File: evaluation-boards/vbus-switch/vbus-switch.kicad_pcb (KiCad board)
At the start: 4 copper layers, 74 x 59 mm, 83 parts, among them J1 BANANA, J10 01x02, J11 Conn_02x06_Top_Bottom, J2 BANANA, J3 BANANA, J4 USB_C, J5 USB_C, J6 USB_A, J7 01x02, J8 01x02, J9 01x02, Q1 PMOS, Q2 PMOS, Q3 PMOS, Q4 PMOS, Q5 2PMOS, Q6 2NMOS, Q7 2NMOS, U1 PAC195X-1-WLCSP, U2 FUSB302BMPX

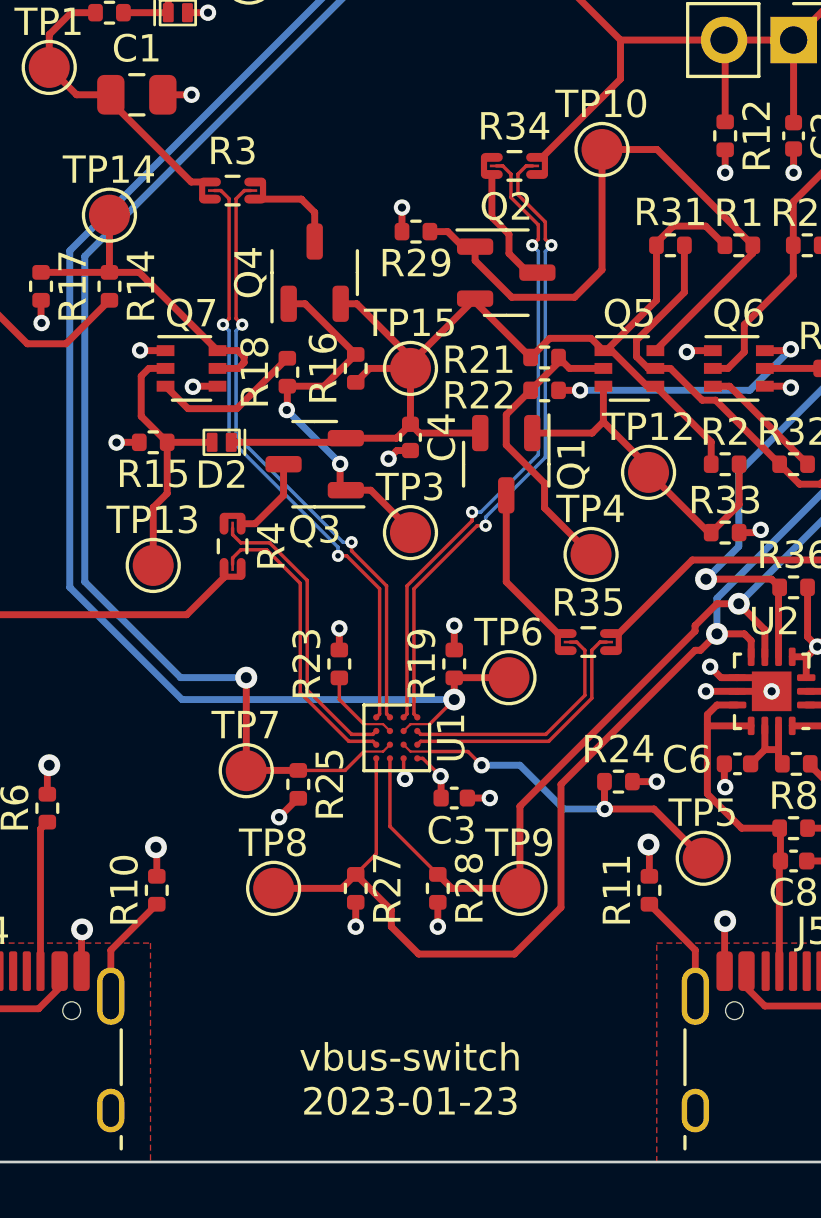
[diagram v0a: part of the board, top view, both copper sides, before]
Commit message: vbus-switch: up minimum trace/space to 3.5 mil
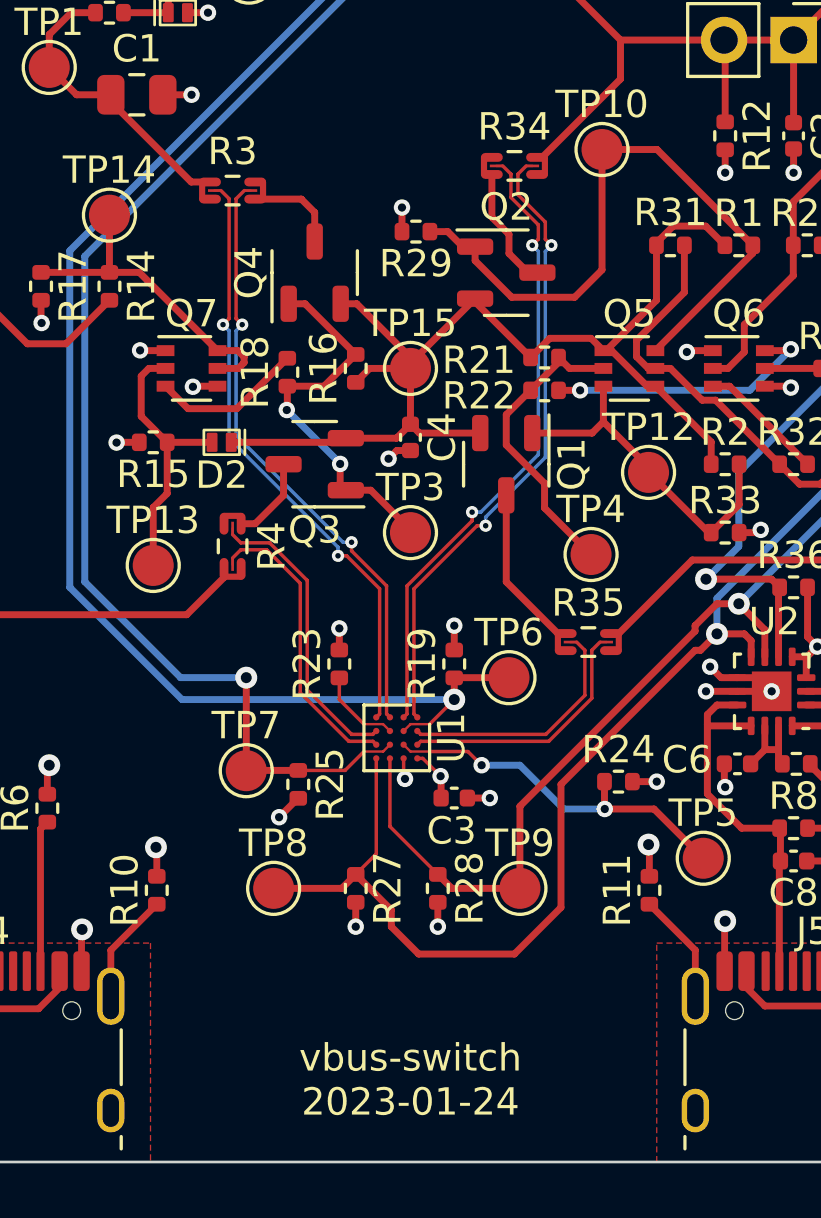
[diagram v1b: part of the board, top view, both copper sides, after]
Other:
- board text added: "vbus-switch 2023-01-24"
- board text removed: "vbus-switch 2023-01-23"
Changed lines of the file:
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@@
     (effects (font (size 2 2) (thickness 0.3)))
   )
-  (gr_text "vbus-switch\n2023-01-23" (at 150 119) (layer "F.SilkS")
+  (gr_text "vbus-switch\n2023-01-24" (at 150 119) (layer "F.SilkS")
     (effects (font (size 1 1) (thickness 0.15)))
   )
@@
   (segment (start 143.92 92.58) (end 143.69 92.35) (width 0.254) (layer "F.Cu") (net 35))
   (segment (start 147.4 104.31) (end 147.4 105.1) (width 0.127) (layer "F.Cu") (net 36))
-  (segment (start 149 106) (end 148.3 106) (width 0.083) (layer "F.Cu") (net 36))
-  (segment (start 149.25 106.25) (end 149 106) (width 0.083) (layer "F.Cu") (net 36))
+  (segment (start 149 106) (end 148.3 106) (width 0.0889) (layer "F.Cu") (net 36))
   (segment (start 147.4 105.1) (end 148.3 106) (width 0.127) (layer "F.Cu") (net 36))
+  (segment (start 149.25 106.25) (end 149 106) (width 0.0889) (layer "F.Cu") (net 36))
   (segment (start 157.1 109.1) (end 158.9 109.1) (width 0.254) (layer "F.Cu") (net 37))
-  (segment (start 149.75 106.75) (end 150 107) (width 0.083) (layer "F.Cu") (net 37))
+  (segment (start 149.75 106.75) (end 150 107) (width 0.0889) (layer "F.Cu") (net 37))
   (segment (start 152.6 107.5) (end 152.1 107) (width 0.127) (layer "F.Cu") (net 37))
-  (segment (start 150 107) (end 150.7 107) (width 0.083) (layer "F.Cu") (net 37))
+  (segment (start 150 107) (end 150.7 107) (width 0.0889) (layer "F.Cu") (net 37))
   (segment (start 157.09 109.09) (end 157.1 109.1) (width 0.254) (layer "F.Cu") (net 37))
   (segment (start 158.9 109.1) (end 160.7 110.9) (width 0.254) (layer "F.Cu") (net 37))
@@
   (segment (start 160.8 100.7) (end 162 99.5) (width 0.254) (layer "B.Cu") (net 41))
   (segment (start 151.6 105.1) (end 150.7 106) (width 0.127) (layer "F.Cu") (net 42))
-  (segment (start 149.75 106.25) (end 150 106) (width 0.083) (layer "F.Cu") (net 42))
+  (segment (start 149.75 106.25) (end 150 106) (width 0.0889) (layer "F.Cu") (net 42))
   (segment (start 153.6 104.3) (end 151.61 104.3) (width 0.254) (layer "F.Cu") (net 42))
   (segment (start 151.6 104.31) (end 151.6 105.1) (width 0.254) (layer "F.Cu") (net 42))
-  (segment (start 150 106) (end 150.7 106) (width 0.083) (layer "F.Cu") (net 42))
+  (segment (start 150 106) (end 150.7 106) (width 0.0889) (layer "F.Cu") (net 42))
   (segment (start 151.61 104.3) (end 151.6 104.31) (width 0.254) (layer "F.Cu") (net 42))
   (via (at 151.6 105.1) (size 0.8) (drill 0.4) (layers "F.Cu" "B.Cu") (net 42))
@@
   (segment (start 145.9 107.69) (end 147.61 107.69) (width 0.127) (layer "F.Cu") (net 43))
   (segment (start 144 107.7) (end 144.01 107.69) (width 0.254) (layer "F.Cu") (net 43))
-  (segment (start 149.25 106.75) (end 149 107) (width 0.083) (layer "F.Cu") (net 43))
+  (segment (start 149.25 106.75) (end 149 107) (width 0.0889) (layer "F.Cu") (net 43))
   (segment (start 144 104.3) (end 144 107.7) (width 0.254) (layer "F.Cu") (net 43))
-  (segment (start 149 107) (end 148.3 107) (width 0.083) (layer "F.Cu") (net 43))
+  (segment (start 149 107) (end 148.3 107) (width 0.0889) (layer "F.Cu") (net 43))
   (segment (start 147.61 107.69) (end 148.3 107) (width 0.127) (layer "F.Cu") (net 43))
   (via (at 144 104.3) (size 0.8) (drill 0.4) (layers "F.Cu" "B.Cu") (net 43))
@@
   (segment (start 148.872999 101.052605) (end 147.667882 99.847488) (width 0.127) (layer "F.Cu") (net 55))
   (segment (start 147.667882 99.847488) (end 147.352512 99.847488) (width 0.127) (layer "F.Cu") (net 55))
-  (segment (start 142.8375 86.5) (end 143.073 86.5) (width 0.127) (layer "F.Cu") (net 55))
+  (segment (start 142.8375 86.5) (end 143.073 86.5) (width 0.0889) (layer "F.Cu") (net 55))
   (segment (start 143.15 91.4) (end 143.372999 91.177001) (width 0.127) (layer "F.Cu") (net 55))
   (segment (start 143.372999 91.177001) (end 143.373 86.8) (width 0.127) (layer "F.Cu") (net 55))
@@
   (segment (start 149.25 105.75) (end 149.127001 105.627001) (width 0.127) (layer "F.Cu") (net 56))
   (segment (start 147.847488 99.667882) (end 147.847488 99.352512) (width 0.127) (layer "F.Cu") (net 56))
-  (segment (start 144.1625 86.5) (end 143.927 86.5) (width 0.127) (layer "F.Cu") (net 56))
+  (segment (start 144.1625 86.5) (end 143.927 86.5) (width 0.0889) (layer "F.Cu") (net 56))
   (segment (start 143.927 86.5) (end 143.627 86.8) (width 0.127) (layer "F.Cu") (net 56))
   (segment (start 149.127001 100.947395) (end 147.847488 99.667882) (width 0.127) (layer "F.Cu") (net 56))
@@
   (segment (start 146.227 100.747394) (end 144.852606 99.373) (width 0.127) (layer "F.Cu") (net 57))
   (segment (start 146.227 104.747394) (end 146.227 100.747394) (width 0.127) (layer "F.Cu") (net 57))
-  (segment (start 143.5 98.8375) (end 143.5 99.073) (width 0.127) (layer "F.Cu") (net 57))
+  (segment (start 143.5 98.8375) (end 143.5 99.073) (width 0.0889) (layer "F.Cu") (net 57))
   (segment (start 143.5 99.073) (end 143.8 99.373) (width 0.127) (layer "F.Cu") (net 57))
   (segment (start 147.852605 106.372999) (end 146.227 104.747394) (width 0.127) (layer "F.Cu") (net 57))
@@
   (segment (start 145.973 104.852606) (end 145.973 100.852606) (width 0.127) (layer "F.Cu") (net 58))
   (segment (start 147.747395 106.627001) (end 145.973 104.852606) (width 0.127) (layer "F.Cu") (net 58))
-  (segment (start 143.5 100.1625) (end 143.5 99.927) (width 0.127) (layer "F.Cu") (net 58))
+  (segment (start 143.5 100.1625) (end 143.5 99.927) (width 0.0889) (layer "F.Cu") (net 58))
   (segment (start 148.627001 106.627001) (end 147.747395 106.627001) (width 0.127) (layer "F.Cu") (net 58))
   (segment (start 152.252512 98.567882) (end 152.252512 98.252512) (width 0.127) (layer "F.Cu") (net 59))
@@
   (segment (start 153.373 85.6) (end 153.673 85.9) (width 0.127) (layer "F.Cu") (net 59))
   (segment (start 149.872999 100.947395) (end 152.252512 98.567882) (width 0.127) (layer "F.Cu") (net 59))
-  (segment (start 153.1375 85.6) (end 153.373 85.6) (width 0.127) (layer "F.Cu") (net 59))
+  (segment (start 153.1375 85.6) (end 153.373 85.6) (width 0.0889) (layer "F.Cu") (net 59))
   (segment (start 149.75 105.75) (end 149.872999 105.627001) (width 0.127) (layer "F.Cu") (net 59))
   (via (at 154.45 88.5) (size 0.45) (drill 0.2) (layers "F.Cu" "B.Cu") (net 59))
@@
   (segment (start 154.227 85.6) (end 153.927 85.9) (width 0.127) (layer "F.Cu") (net 60))
   (segment (start 154.927001 87.647395) (end 153.927 86.647394) (width 0.127) (layer "F.Cu") (net 60))
-  (segment (start 154.4625 85.6) (end 154.227 85.6) (width 0.127) (layer "F.Cu") (net 60))
+  (segment (start 154.4625 85.6) (end 154.227 85.6) (width 0.0889) (layer "F.Cu") (net 60))
   (segment (start 154.927001 88.277001) (end 154.927001 87.647395) (width 0.127) (layer "F.Cu") (net 60))
   (segment (start 155.15 88.5) (end 154.927001 88.277001) (width 0.127) (layer "F.Cu") (net 60))
@@
   (segment (start 152.747488 98.432118) (end 154.927001 96.252605) (width 0.127) (layer "B.Cu") (net 60))
   (segment (start 154.927001 88.722999) (end 155.15 88.5) (width 0.127) (layer "B.Cu") (net 60))
-  (segment (start 155.8375 103) (end 156.073 103) (width 0.127) (layer "F.Cu") (net 61))
+  (segment (start 155.8375 103) (end 156.073 103) (width 0.0889) (layer "F.Cu") (net 61))
   (segment (start 156.073 103) (end 156.373 103.3) (width 0.127) (layer "F.Cu") (net 61))
   (segment (start 150.25 106.25) (end 150.372999 106.372999) (width 0.127) (layer "F.Cu") (net 61))
@@
   (segment (start 154.947395 106.372999) (end 156.373 104.947394) (width 0.127) (layer "F.Cu") (net 61))
   (segment (start 156.373 104.947394) (end 156.373 103.3) (width 0.127) (layer "F.Cu") (net 61))
-  (segment (start 157.1625 103) (end 156.927 103) (width 0.127) (layer "F.Cu") (net 62))
+  (segment (start 157.1625 103) (end 156.927 103) (width 0.0889) (layer "F.Cu") (net 62))
   (segment (start 150.372999 106.627001) (end 155.052605 106.627001) (width 0.127) (layer "F.Cu") (net 62))
   (segment (start 150.25 106.75) (end 150.372999 106.627001) (width 0.127) (layer "F.Cu") (net 62))

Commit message: vbus-switch: add part selections
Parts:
- R20, R30: value R -> 10k
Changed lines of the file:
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@@
       (effects (font (size 1 1) (thickness 0.15)))
     )
-    (fp_text value "R" (at 0 1.17) (layer "F.Fab")
+    (fp_text value "10k" (at 0 1.17) (layer "F.Fab")
       (effects (font (size 1 1) (thickness 0.15)))
     )
@@
     (descr "SOT, 3 Pin (https://www.jedec.org/sites/default/files/docs/Mo-178D.PDF inferred 3-pin variant), generated with kicad-footprint-generator ipc_gullwing_generator.py")
     (tags "SOT TO_SOT_SMD")
+    (property "Manufacturer" "Panjit")
+    (property "Part Number" "PJA3441_R1_00001")
     (property "Sheetfile" "vbus-switch.kicad_sch")
     (property "Sheetname" "")
@@
     (descr "USB Type-C receptacle for USB 2.0 and PD, http://www.krhro.com/uploads/soft/180320/1-1P320120243.pdf")
     (tags "USB_C female connector receptacle type-c usb-2.0 usb pd")
+    (property "Manufacturer" "XKB")
+    (property "Part Number" "U262-161N-4BVC11")
     (property "Sheetfile" "vbus-switch.kicad_sch")
     (property "Sheetname" "")
@@
     (descr "SOT-363, SC-70-6")
     (tags "SOT-363 SC-70-6")
+    (property "Manufacturer" "Yangzhou Yangjie")
+    (property "Part Number" "BSS84DW")
     (property "Sheetfile" "vbus-switch.kicad_sch")
     (property "Sheetname" "")
@@
     (descr "WLCSP-16, PAC195X, pads sized for 3.5 mil trace/space")
     (tags "WLCSP BGA 16  0.5")
+    (property "Manufacturer" "Microchip")
+    (property "Part Number" "PAC1954T-E/J6CX")
     (property "Sheetfile" "vbus-switch.kicad_sch")
     (property "Sheetname" "")
@@
     (descr "WQFN, 14 Pin (https://www.onsemi.com/pub/Collateral/FUSB302B-D.PDF#page=32), generated with kicad-footprint-generator ipc_noLead_generator.py")
     (tags "WQFN NoLead")
+    (property "Manufacturer" "onsemi")
+    (property "Part Number" "FUSB302BMPX")
     (property "Sheetfile" "vbus-switch.kicad_sch")
     (property "Sheetname" "")
@@
     (descr "SOT, 3 Pin (https://www.jedec.org/sites/default/files/docs/Mo-178D.PDF inferred 3-pin variant), generated with kicad-footprint-generator ipc_gullwing_generator.py")
     (tags "SOT TO_SOT_SMD")
+    (property "Manufacturer" "Panjit")
+    (property "Part Number" "PJA3441_R1_00001")
     (property "Sheetfile" "vbus-switch.kicad_sch")
     (property "Sheetname" "")
@@
     (descr "SOT, 3 Pin (https://www.jedec.org/sites/default/files/docs/Mo-178D.PDF inferred 3-pin variant), generated with kicad-footprint-generator ipc_gullwing_generator.py")
     (tags "SOT TO_SOT_SMD")
+    (property "Manufacturer" "Panjit")
+    (property "Part Number" "PJA3441_R1_00001")
     (property "Sheetfile" "vbus-switch.kicad_sch")
     (property "Sheetname" "")
@@
     (descr "SOT-363, SC-70-6")
     (tags "SOT-363 SC-70-6")
+    (property "Manufacturer" "Yangzhou Yangjie")
+    (property "Part Number" "2N7002DW")
     (property "Sheetfile" "vbus-switch.kicad_sch")
     (property "Sheetname" "")
@@
     (descr "SOT-363, SC-70-6")
     (tags "SOT-363 SC-70-6")
+    (property "Manufacturer" "Yangzhou Yangjie")
+    (property "Part Number" "2N7002DW")
     (property "Sheetfile" "vbus-switch.kicad_sch")
     (property "Sheetname" "")
@@
     (descr "USB Type-C receptacle for USB 2.0 and PD, http://www.krhro.com/uploads/soft/180320/1-1P320120243.pdf")
     (tags "USB_C female connector receptacle type-c usb-2.0 usb pd")
+    (property "Manufacturer" "XKB")
+    (property "Part Number" "U262-161N-4BVC11")
     (property "Sheetfile" "vbus-switch.kicad_sch")
     (property "Sheetname" "")
@@
       (effects (font (size 1 1) (thickness 0.15)))
     )
-    (fp_text value "R" (at 0 1.17) (layer "F.Fab")
+    (fp_text value "10k" (at 0 1.17) (layer "F.Fab")
       (effects (font (size 1 1) (thickness 0.15)))
     )
@@
     (descr "SOT, 3 Pin (https://www.jedec.org/sites/default/files/docs/Mo-178D.PDF inferred 3-pin variant), generated with kicad-footprint-generator ipc_gullwing_generator.py")
     (tags "SOT TO_SOT_SMD")
+    (property "Manufacturer" "Panjit")
+    (property "Part Number" "PJA3441_R1_00001")
     (property "Sheetfile" "vbus-switch.kicad_sch")
     (property "Sheetname" "")
@@
     (descr "USB A connector http://www.kycon.com/Pub_Eng_Draw/KUSBXHT-SB-AS1N-B30-NF.pdf")
     (tags "USB_A female connector receptacle type-a usb-2.0")
-    (property "Sheetfile" "vbus-switch.kicad_sch")
-    (property "Sheetname" "")
+    (property "Manufacturer" "Jing Extension of the Electronic Co.")
+    (property "Part Number" "C42411")
+    (property "Sheetfile" "vbus-switch.kicad_sch")
+    (property "Sheetname" "")
